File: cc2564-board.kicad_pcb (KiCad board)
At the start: 4 copper layers, 25.9 x 67.9 mm, 72 parts, among them J1 TYPE-C-31-M-12, J2 Conn_ARM_JTAG_SWD_10, J3 Conn_01x16, J4 Conn_01x16, J5 BOOT, J6 1909763-1, J7 Conn_01x04, SW1 SW_Push, U1 TLV7111833DDSET, U2 USBLC6-2P6, U4 STM32F103C8Tx, U5 TXB0104D, U6 TXB0104D, U7 CC2564CRVMR, Y1 ECS-80-18-30-JGN-TR, Y2 ECS-327MVATX-3-CN-TR

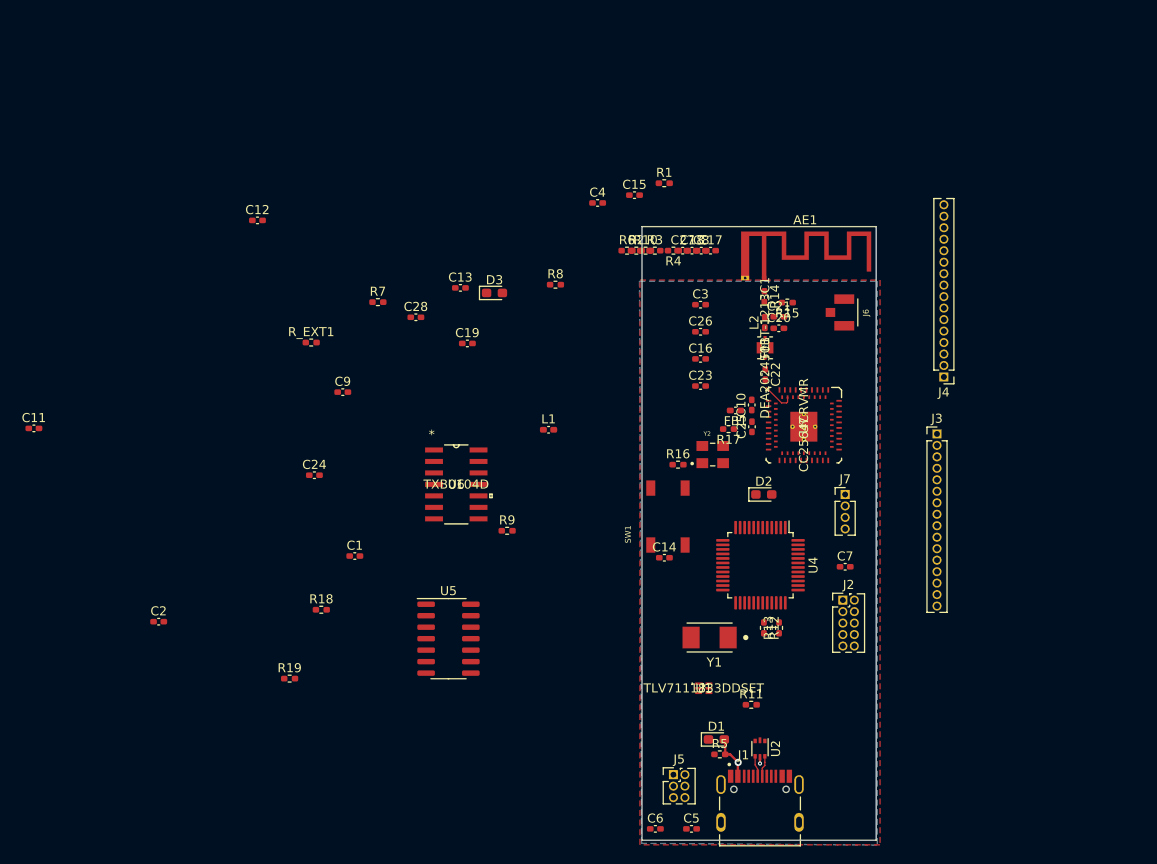
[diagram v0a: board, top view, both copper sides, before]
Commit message: More board setup pain, route BT fast clock
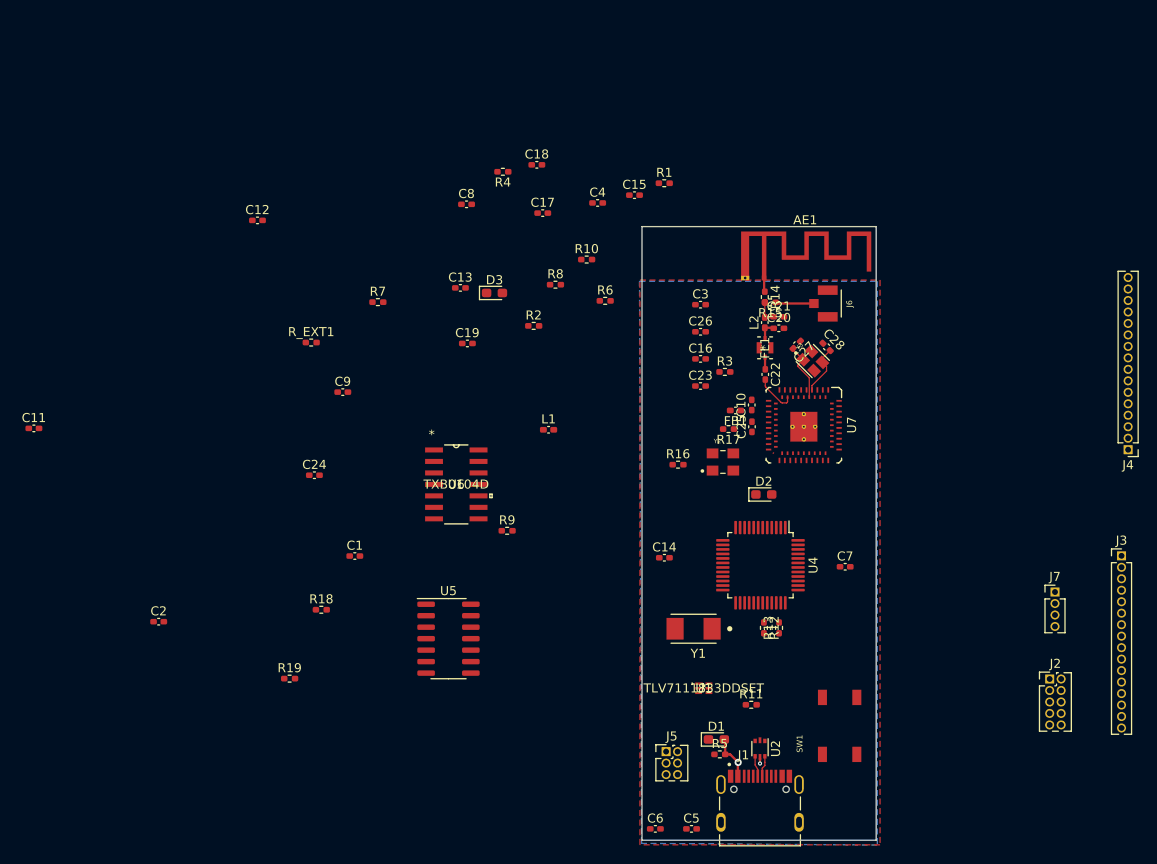
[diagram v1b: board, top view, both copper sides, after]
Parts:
- added Y3: ECS-260-8-36CKM-TR, cc2654-board-footprints:XTAL_ECS-260-8-36CKM-TR, F.Cu at (196.4, 90.2)
- moved C28 45.6 mm to (197.9, 88.7), turned to -45 degrees
- moved SW1 30.0 mm to (199.4, 130.6)
- moved C8 26.5 mm to (158.1, 72.9)
- moved J7 25.6 mm to (223.2, 115.8)
- moved J2 24.5 mm to (222.6, 125.4)
- moved J3 24.5 mm to (230.6, 111.8)
- moved J4 21.9 mm to (231.3, 100.0)
- moved R4 20.8 mm to (162.1, 69.3)
- moved C18 19.6 mm to (165.9, 68.5)
- moved C17 19.0 mm to (166.5, 73.9)
- moved C27 16.4 mm to (194.6, 88.4), turned to -135 degrees
- moved R3 15.5 mm to (186.7, 91.4)
- moved R2 14.1 mm to (165.5, 86.3)
- moved R10 6.59 mm to (171.4, 79.0)
- moved R6 6.06 mm to (173.4, 83.6)
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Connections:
- C27 pad 2: GND -> Net-(C27-Pad2)
- J1 pad A8: no_connect_81 -> no_connect_79
- J1 pad B8: no_connect_82 -> no_connect_80
- J2 pad 8: no_connect_83 -> no_connect_81
- U4 pad 2: no_connect_84 -> no_connect_82
- U4 pad 3: no_connect_85 -> no_connect_83
- U4 pad 4: no_connect_86 -> no_connect_84
- U5 pad 10: no_connect_87 -> no_connect_85
- U5 pad 11: no_connect_88 -> no_connect_86
- U5 pad 12: no_connect_89 -> no_connect_87
- U5 pad 3: no_connect_90 -> no_connect_88
- U5 pad 4: no_connect_91 -> no_connect_89
- U5 pad 5: no_connect_92 -> no_connect_90
- U7 pad A1: no_connect_93 -> no_connect_91
- U7 pad A12: no_connect_94 -> no_connect_92
- U7 pad A13: no_connect_95 -> no_connect_93
- U7 pad A14: no_connect_96 -> no_connect_94
- U7 pad A15: no_connect_97 -> no_connect_95
- U7 pad A16: no_connect_98 -> no_connect_96
- U7 pad A18: no_connect_99 -> no_connect_97
- U7 pad A19: no_connect_100 -> no_connect_98
- U7 pad A2: Net-(U7-PadA2) -> no_connect_99
- U7 pad A20: no_connect_101 -> no_connect_100
- U7 pad A21: no_connect_102 -> no_connect_101
- U7 pad A22: no_connect_103 -> no_connect_102
- U7 pad A23: no_connect_104 -> no_connect_103
- U7 pad A27: no_connect_105 -> no_connect_104
- U7 pad A3: Net-(U7-PadA2) -> no_connect_105
- U7 pad A5: Net-(U7-PadA5) -> no_connect_113
- U7 pad A7: no_connect_113 -> no_connect_114
- U7 pad A8: no_connect_114 -> no_connect_115
- U7 pad A9: Net-(U7-PadA5) -> no_connect_116
- U7 pad B1: no_connect_115 -> no_connect_117
- U7 pad B10: no_connect_116 -> no_connect_118
- U7 pad B12: no_connect_117 -> no_connect_119
- U7 pad B13: no_connect_118 -> no_connect_120
- U7 pad B14: no_connect_119 -> no_connect_121
- U7 pad B15: Net-(U7-PadA2) -> no_connect_122
- U7 pad B16: no_connect_120 -> no_connect_123
- U7 pad B17: no_connect_121 -> no_connect_124
- U7 pad B2: Net-(U7-PadA5) -> no_connect_125
- U7 pad B20: no_connect_122 -> no_connect_126
- U7 pad B23: no_connect_123 -> no_connect_127
- U7 pad B26: Net-(U7-PadA2) -> no_connect_128
- U7 pad B27: Net-(U7-PadA2) -> no_connect_129
- U7 pad B28: no_connect_124 -> no_connect_130
- U7 pad B29: no_connect_125 -> no_connect_131
- U7 pad B30: no_connect_126 -> no_connect_132
- U7 pad B31: no_connect_127 -> no_connect_133
- U7 pad B32: no_connect_128 -> no_connect_134
- U7 pad B33: no_connect_129 -> no_connect_135
- U7 pad B34: no_connect_130 -> no_connect_136
- U7 pad B35: Net-(U7-PadA2) -> no_connect_137
- U7 pad B36: Net-(U7-PadA2) -> no_connect_138
- U7 pad B4: GND -> Net-(C27-Pad2)
- U7 pad B5: Net-(U7-PadB5) -> no_connect_139
- U7 pad B6: Net-(U7-PadB5) -> no_connect_140
- U7 pad B7: Net-(U7-PadA5) -> no_connect_141
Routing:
- net Net-(C27-Pad2): track 0.00 -> 6.62 mm
- net Net-(C28-Pad2): track 0.00 -> 5.58 mm
- net Net-(J6-Pad1): track 0.00 -> 4.29 mm
- net Net-(C21-Pad1): track 0.00 -> 2.67 mm
- net Net-(C20-Pad1): track 0.00 -> 2.21 mm
- net Net-(AE1-Pad1): track 0.00 -> 1.54 mm
- net Net-(C22-Pad1): track 0.00 -> 1.36 mm
- net Net-(C22-Pad2): track 3.68 -> 4.57 mm

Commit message: Swap out level shifters for one 8 channel QFN
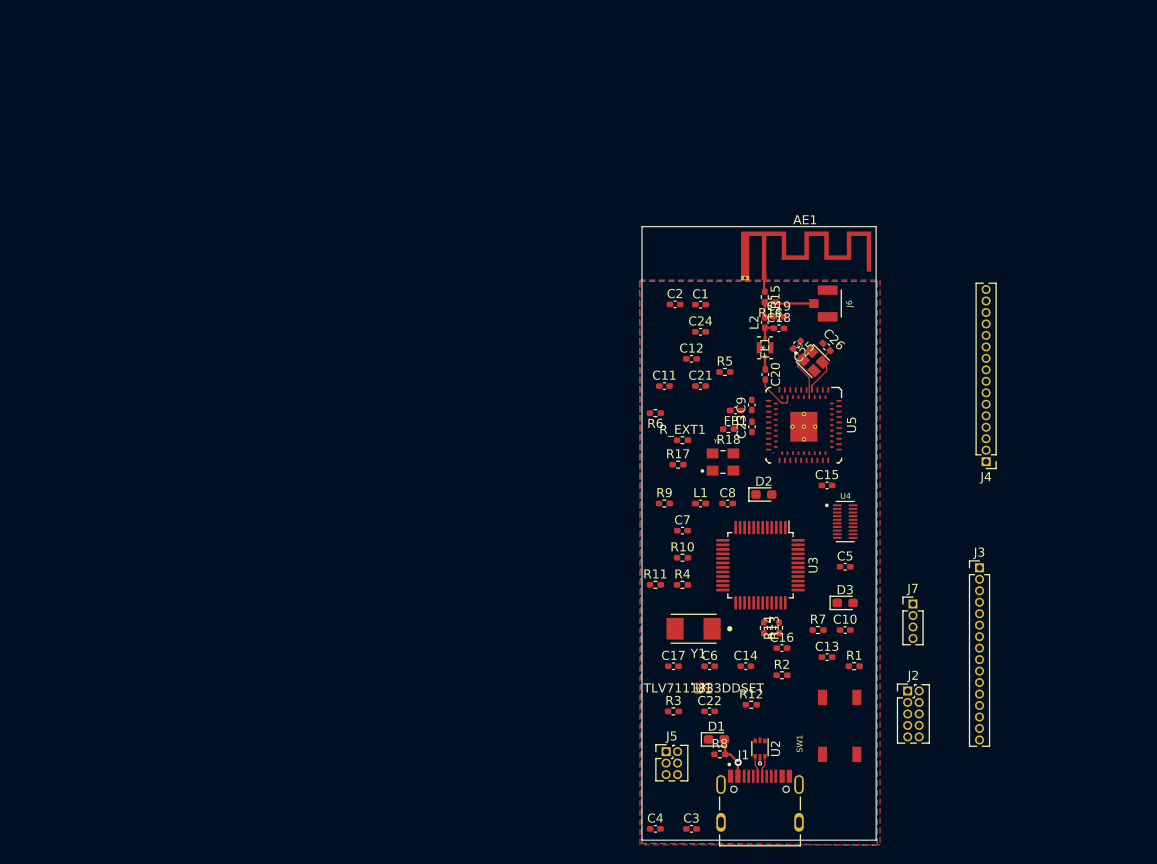
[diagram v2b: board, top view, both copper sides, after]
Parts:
- removed the C16 at (184.0, 90.0)
- removed the C17 at (166.5, 73.9)
- removed the R8 at (167.9, 81.8)
- removed the R9 at (162.6, 109.0)
- removed the U5 at (156.1, 121.0)
- removed U6: TXB0104D, cc2654-board-footprints:TXB0104D
- added R7: 10k, Resistor_SMD:R_0402_1005Metric_Pad0.72x0.64mm_HandSolder, F.Cu at (197.0, 120.0)
- added U4: TXB0108DQSR, cc2654-board-footprints:TXB0108DQSR, F.Cu at (200.0, 108.0)
- moved C10 76.0 mm to (200.0, 120.0)
- moved C11 69.9 mm to (180.0, 93.0)
- moved C16 60.0 mm to (193.0, 122.0)
- moved C13 57.6 mm to (198.0, 123.0)
- moved R2 56.0 mm to (193.0, 125.0)
- moved D3 51.8 mm to (200.0, 117.0)
- moved R1 51.7 mm to (201.0, 124.0)
- moved C22 50.9 mm to (185.0, 129.0)
- moved C12 50.4 mm to (183.0, 90.0)
- moved R4 44.7 mm to (182.0, 115.0)
- moved C8 44.3 mm to (187.0, 106.0)
- moved R10 44.0 mm to (182.0, 112.0)
- moved C7 43.3 mm to (182.0, 109.0)
- moved R_EXT1 42.5 mm to (182.0, 99.0)
- moved C17 42.4 mm to (181.0, 124.0)
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- renumbered C3 to C1, C2 to C10, C18 to C16, C19 to C17, C20 to C18, C21 to C19, C4 to C2, C22 to C20, C23 to C21, C24 to C22, C25 to C23, C26 to C24, C27 to C25, C28 to C26, C5 to C3, C6 to C4, C7 to C5, C1 to C6, C8 to C7, C9 to C8, C10 to C9, R2 to R1, R7 to R10, R10 to R11, R11 to R12, R12 to R13, R13 to R14, R14 to R15, R15 to R16, R16 to R17, R17 to R18, R1 to R2, R18 to R3, R19 to R4, R3 to R5, R4 to R6, R5 to R8, R6 to R9, U4 to U3, U7 to U5
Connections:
- C14 pad 2: VDD_3V3 -> VDD_1V8
- C15 pad 2: VDD_1V8 -> VDD_3V3
- J1 pad A8: no_connect_79 -> no_connect_78
- J1 pad B8: no_connect_80 -> no_connect_79
- J2 pad 8: no_connect_81 -> no_connect_80
- U3 pad 2: no_connect_82 -> no_connect_81
- U3 pad 3: no_connect_83 -> no_connect_82
- U3 pad 4: no_connect_84 -> no_connect_83
- U5 pad A1: no_connect_91 -> no_connect_90
- U5 pad A12: no_connect_92 -> no_connect_91
- U5 pad A13: no_connect_93 -> no_connect_92
- U5 pad A14: no_connect_94 -> no_connect_93
- U5 pad A15: no_connect_95 -> no_connect_94
- U5 pad A16: no_connect_96 -> no_connect_95
- U5 pad A18: no_connect_97 -> no_connect_96
- U5 pad A19: no_connect_98 -> no_connect_97
- U5 pad A2: no_connect_99 -> no_connect_98
- U5 pad A20: no_connect_100 -> no_connect_99
- U5 pad A21: no_connect_101 -> no_connect_100
- U5 pad A22: no_connect_102 -> no_connect_101
- U5 pad A23: no_connect_103 -> no_connect_102
- U5 pad A27: no_connect_104 -> no_connect_103
- U5 pad A3: no_connect_105 -> no_connect_104
- U5 pad A30: no_connect_106 -> no_connect_105
- U5 pad A31: no_connect_107 -> no_connect_106
- U5 pad A35: no_connect_108 -> no_connect_107
- U5 pad A36: no_connect_109 -> no_connect_108
- U5 pad A37: no_connect_110 -> no_connect_109
- U5 pad A39: no_connect_111 -> no_connect_110
- U5 pad A40: no_connect_112 -> no_connect_111
- U5 pad A5: no_connect_113 -> no_connect_112
- U5 pad A7: no_connect_114 -> no_connect_113
- U5 pad A8: no_connect_115 -> no_connect_114
- U5 pad A9: no_connect_116 -> no_connect_115
- U5 pad B1: no_connect_117 -> no_connect_116
- U5 pad B10: no_connect_118 -> no_connect_117
- U5 pad B12: no_connect_119 -> no_connect_118
- U5 pad B13: no_connect_120 -> no_connect_119
- U5 pad B14: no_connect_121 -> no_connect_120
- U5 pad B15: no_connect_122 -> no_connect_121
- U5 pad B16: no_connect_123 -> no_connect_122
- U5 pad B17: no_connect_124 -> no_connect_123
- U5 pad B2: no_connect_125 -> no_connect_124
- U5 pad B20: no_connect_126 -> no_connect_125
- U5 pad B23: no_connect_127 -> no_connect_126
- U5 pad B26: no_connect_128 -> no_connect_127
- U5 pad B27: no_connect_129 -> no_connect_128
- U5 pad B28: no_connect_130 -> no_connect_129
- U5 pad B29: no_connect_131 -> no_connect_130
- U5 pad B30: no_connect_132 -> no_connect_131
- U5 pad B31: no_connect_133 -> no_connect_132
- U5 pad B32: no_connect_134 -> no_connect_133
- U5 pad B33: no_connect_135 -> no_connect_134
- U5 pad B34: no_connect_136 -> no_connect_135
- U5 pad B35: no_connect_137 -> no_connect_136
- U5 pad B36: no_connect_138 -> no_connect_137
- U5 pad B5: no_connect_139 -> no_connect_138
- U5 pad B6: no_connect_140 -> no_connect_139
- U5 pad B7: no_connect_141 -> no_connect_140

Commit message: Begin serious layout
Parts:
- moved C22 53.8 mm to (183.0, 75.2)
- moved J7 45.6 mm to (182.9, 78.8)
- moved C3 42.4 mm to (166.9, 102.8)
- moved C4 42.2 mm to (167.0, 101.5), turned to 180 degrees
- moved C14 40.7 mm to (169.3, 88.4)
- moved J4 40.2 mm to (196.6, 65.9), turned to 0 degrees
- moved C13 40.1 mm to (172.5, 92.1)
- moved R7 39.4 mm to (175.0, 87.4), turned to 180 degrees
- moved D3 39.2 mm to (162.1, 107.2), turned to 180 degrees
- moved J5 38.9 mm to (161.2, 99.5)
- moved C10 37.2 mm to (164.4, 109.4), turned to -90 degrees
- moved C5 36.8 mm to (164.3, 104.0)
- moved J2 34.7 mm to (177.4, 108.5), turned to 90 degrees
- moved U4 34.1 mm to (172.2, 88.2), turned to 180 degrees
- moved C9 32.9 mm to (165.7, 72.5)
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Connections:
- U2 pad 1: USB_D- -> USB_D+
- U2 pad 3: USB_D+ -> USB_D-
- U2 pad 4: USB_CONN_D+ -> USB_CONN_D-
- U2 pad 6: USB_CONN_D- -> USB_CONN_D+
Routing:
- net VDD_1V8: track 0.06 -> 28.8 mm, vias 0 -> 2
- net VCC_USB: track 1.97 -> 10.3 mm, vias 2 -> 6
- net USB_D+: track 0.00 -> 4.09 mm
- net USB_CONN_D-: track 2.33 -> 6.23 mm
- net Net-(J1-PadA5): track 0.00 -> 3.14 mm
- net USB_CONN_D+: track 2.29 -> 5.23 mm
- net Net-(J1-PadB5): track 0.00 -> 2.90 mm
- net USB_D-: track 0.00 -> 2.80 mm
- net SWD_NRST: track 0.00 -> 2.19 mm
- net Net-(D1-Pad2): track 3.50 -> 1.86 mm
- net Net-(R4-Pad1): track 0.00 -> 1.51 mm
- net Net-(R3-Pad1): track 0.00 -> 1.44 mm
- net GND: vias 0 -> 7
- net (no net): vias 0 -> 5
- added copper zone on In2.Cu, net VCC_USB
- added copper zone on In2.Cu, net VDD_1V8
- added copper zone on In2.Cu, net VDD_3V3
- removed copper zone on B.Cu, net GND
